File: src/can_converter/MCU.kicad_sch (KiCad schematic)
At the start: 12 parts, among them P2 CONN_01X02, U1 STM32G0B1CBT, X3 TC2030-NL, Y1 830108313809

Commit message: Add jst pa connector, replace tranciever, replace componenets, remove unneeded files
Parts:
- removed X3: TC2030-NL, Connector_Tag-Connect:TC2030-NL, symbol tag-connect:TC2030-NL
- added J102: IDC6, Bluesat:IDC6, symbol Connector_Generic:Conn_02x03_Odd_Even
- C1, C2: footprint Capacitor_SMD:C_0402_1005Metric_Pad0.74x0.62mm_HandSolder -> Capacitor_SMD:C_0402_1005Metric
- C3, C4, C5: footprint Capacitor_SMD:C_0603_1608Metric_Pad1.08x0.95mm_HandSolder -> Capacitor_SMD:C_0402_1005Metric
- R6: footprint Resistor_SMD:R_0402_1005Metric_Pad0.72x0.64mm_HandSolder -> Resistor_SMD:R_0402_1005Metric
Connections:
- net +3V3: now also J102.4 (Pin_4)
- net GND: now also J102.3 (Pin_3)
- net NRST: now also J102.6 (Pin_6)
- net SWCLK: now also J102.2 (Pin_2)
- net SWDIO: now also J102.1 (Pin_1)
- no-connect marks 28 -> 27

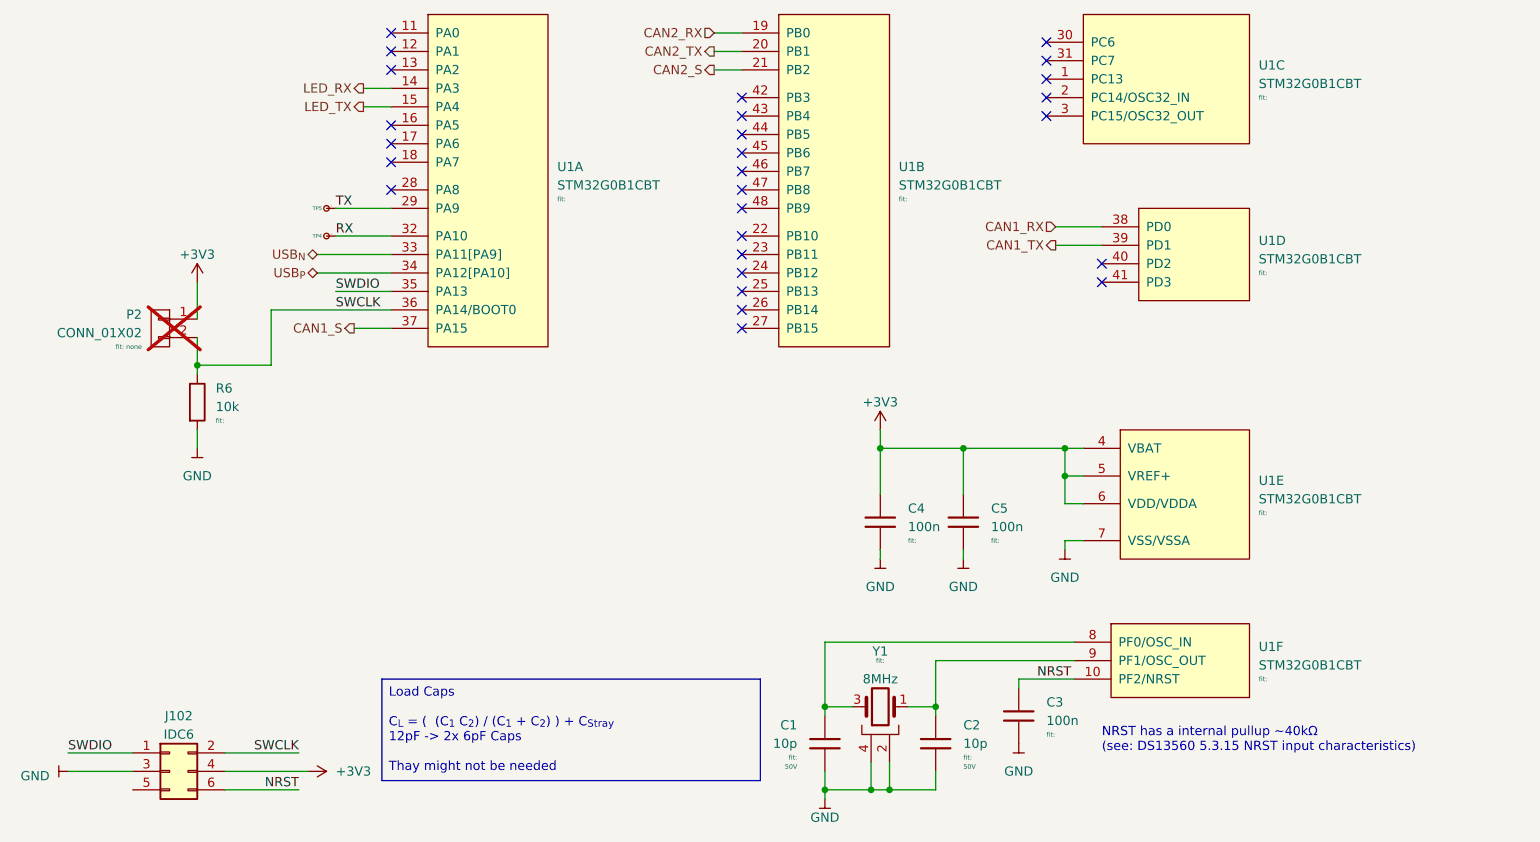
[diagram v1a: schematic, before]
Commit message: Remove lockfile, remove old debug header, route new debug header
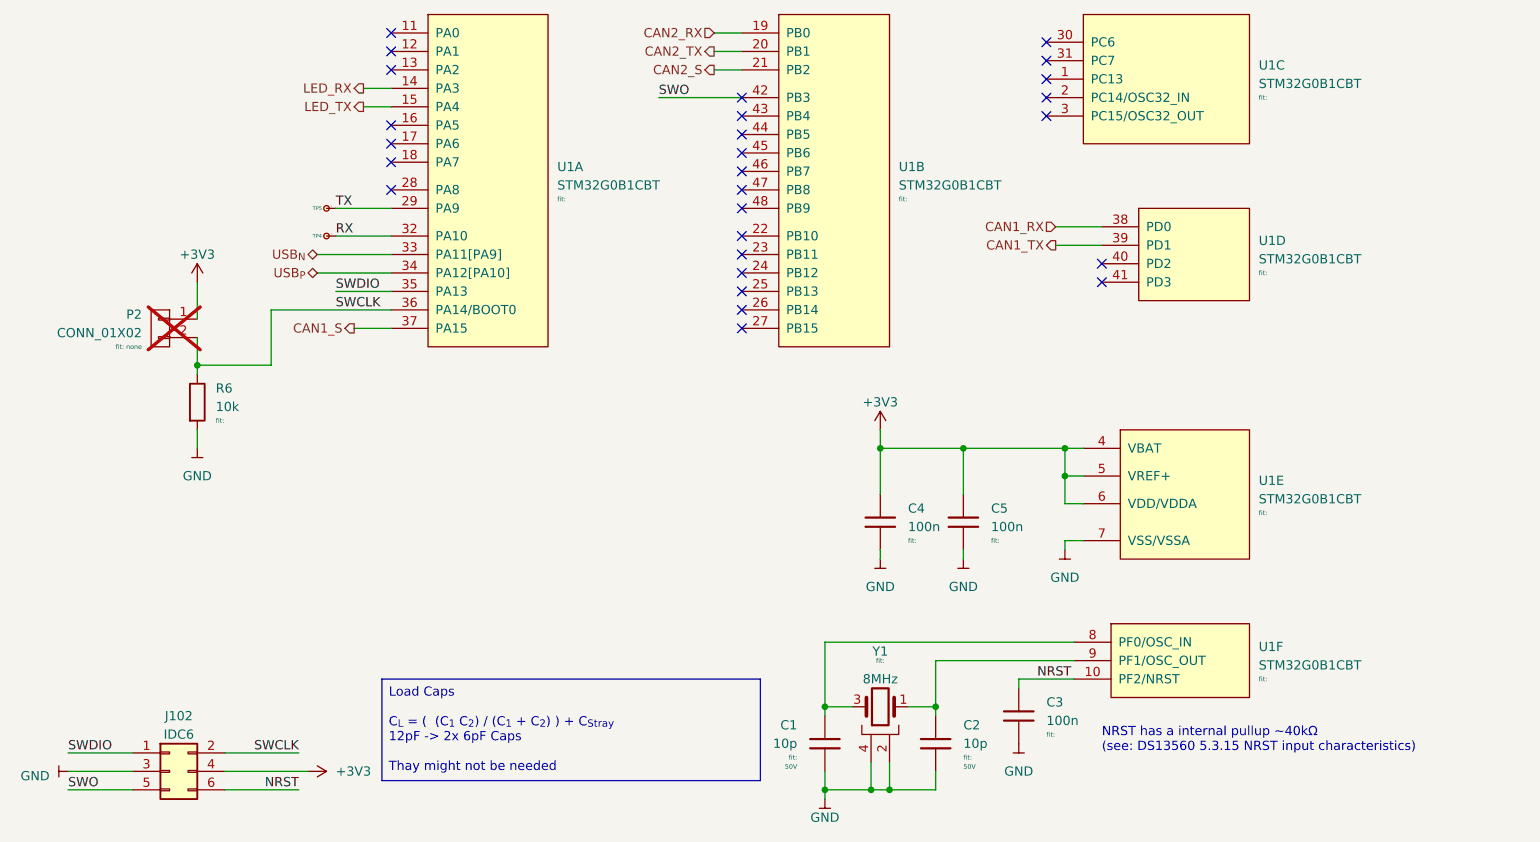
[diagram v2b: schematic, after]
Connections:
- net SWO: now reaches J102.5 (Pin_5)
- net SWO: now also U1.42 (PB3)
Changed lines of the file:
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@@
+	(wire
+		(pts
+			(xy 22.86 123.19) (xy 31.75 123.19)
+		)
+		(stroke
+			(width 0)
+			(type default)
+		)
+	)
 	(wire
 		(pts
@@
 		(pts
 			(xy 160.02 90.17) (xy 160.02 88.9)
+		)
+		(stroke
+			(width 0)
+			(type default)
+		)
+	)
+	(wire
+		(pts
+			(xy 104.14 27.94) (xy 115.57 27.94)
 		)
 		(stroke
@@
 		)
 	)
+	(label "SWO"
+		(at 22.86 123.19 0)
+		(effects
+			(font
+				(size 1.27 1.27)
+			)
+			(justify left bottom)
+		)
+	)
 	(label "SWDIO"
 		(at 59.69 54.61 0)
 		(effects
 			(font
+				(size 1.27 1.27)
+			)
+			(justify left bottom)
+		)
+	)
+	(label "SWO"
+		(at 104.14 27.94 0)
+		(effects
+			(font

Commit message: Finish layout and routing
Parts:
- removed P2: CONN_01X02, Connector_generic:Header_1x2_Pitch2.54mm, symbol generic-connectors:CONN_01X02
- C4: value 100n -> 220n; Package 0603 -> 0402
- C5: value 100n -> 220n
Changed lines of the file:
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@@
-	)
-	(junction
-		(at 40.64 64.77)
-		(diameter 0)
-		(color 0 0 0 0)
 	)
 	(junction
@@
 	(wire
 		(pts
-			(xy 40.64 64.77) (xy 50.8 64.77)
-		)
-		(stroke
-			(width 0)
-			(type default)
-		)
-	)
-	(wire
-		(pts
 			(xy 62.23 59.69) (xy 67.31 59.69)
 		)
@@
 	(wire
 		(pts
+			(xy 40.64 57.15) (xy 40.64 66.04)
+		)
+		(stroke
+			(width 0)
+			(type default)
+		)
+	)
+	(wire
+		(pts
 			(xy 63.5 29.21) (xy 67.31 29.21)
 		)
@@
 	(wire
 		(pts
-			(xy 50.8 64.77) (xy 50.8 57.15)
-		)
-		(stroke
-			(width 0)
-			(type default)
-		)
-	)
-	(wire
-		(pts
 			(xy 135.89 123.19) (xy 142.24 123.19)
 		)
@@
 	(wire
 		(pts
-			(xy 40.64 64.77) (xy 40.64 66.04)
-		)
-		(stroke
-			(width 0)
-			(type default)
-		)
-	)
-	(wire
-		(pts
 			(xy 44.45 118.11) (xy 54.61 118.11)
 		)
@@
 	(wire
 		(pts
-			(xy 50.8 57.15) (xy 67.31 57.15)
-		)
-		(stroke
-			(width 0)
-			(type default)
-		)
-	)
-	(wire
-		(pts
 			(xy 22.86 118.11) (xy 31.75 118.11)
 		)
@@
 	(wire
 		(pts
-			(xy 40.64 53.34) (xy 40.64 58.42)
-		)
-		(stroke
-			(width 0)
-			(type default)
-		)
-	)
-	(wire
-		(pts
 			(xy 160.02 83.82) (xy 160.02 80.01)
 		)
@@
 	(wire
 		(pts
-			(xy 40.64 60.96) (xy 40.64 64.77)
-		)
-		(stroke
-			(width 0)
-			(type default)
-		)
-	)
-	(wire
-		(pts
 			(xy 135.89 119.38) (xy 135.89 123.19)
 		)
@@
 		(pts
 			(xy 146.05 90.17) (xy 146.05 91.44)
+		)
+		(stroke
+			(width 0)
+			(type default)
+		)
+	)
+	(wire
+		(pts
+			(xy 40.64 57.15) (xy 67.31 57.15)
 		)
 		(stroke
@@
 	)
 	(symbol
-		(lib_id "generic-connectors:CONN_01X02")
-		(at 35.56 60.96 0)
-		(mirror y)
-		(unit 1)
-		(exclude_from_sim no)
-		(in_bom yes)
-		(on_board yes)
-		(dnp yes)
-		(fields_autoplaced yes)
-		(property "Reference" "P2"
-			(at 33.02 57.785 0)
-			(effects
-				(font
-					(size 1.27 1.27)
-				)
-				(justify left)
-			)
-		)
-		(property "Value" "CONN_01X02"
-			(at 33.02 60.325 0)
-			(effects
-				(font
-					(size 1.27 1.27)
-				)
-				(justify left)
-			)
-		)
-		(property "Footprint" "Connector_generic:Header_1x2_Pitch2.54mm"
-			(at 46.99 54.61 0)
-			(effects
-				(font
-					(size 1.27 1.27)
-				)
-				(hide yes)
-			)
-		)
-		(property "Datasheet" ""
-			(at 35.56 55.88 0)
-			(effects
-				(font
-					(size 1.27 1.27)
-				)
-			)
-		)
-		(property "Description" ""
-			(at 35.56 60.96 0)
-			(effects
-				(font
-					(size 1.27 1.27)
-				)
-			)
-		)
-		(property "Manufacturer" "generic"
-			(at 33.02 53.34 0)
-			(effects
-				(font
-					(size 1.524 1.524)
-				)
-				(hide yes)
-			)
-		)
-		(property "MPN" "generic"
-			(at 30.48 50.8 0)
-			(effects
-				(font
-					(size 1.524 1.524)
-				)
-				(hide yes)
-			)
-		)
-		(property "Fit" "fit: none"
-			(at 33.02 62.23 0)
-			(effects
-				(font
-					(size 0.635 0.635)
-				)
-				(justify left)
-			)
-		)
-		(property "State" "legacy"
-			(at 27.94 64.77 0)
-			(effects
-				(font
-					(size 0.635 0.635)
-				)
-				(hide yes)
-			)
-		)
-		(property "Package" "THT 2.54mm 1x2-pin"
-			(at 35.56 60.96 0)
-			(effects
-				(font
-					(size 0.635 0.635)
-				)
-				(hide yes)
-			)
-		)
-		(pin "1"
-		)
-		(pin "2"
-		)
-		(instances
-			(project "candleLightfd-S01"
-				(path "/e63e39d7-6ac0-4ffd-8aa3-1841a4541b55/c754f27f-d753-4109-9c59-639a39396c66"
-					(reference "P2")
-					(unit 1)
-				)
-			)
-		)
-	)
-	(symbol
 		(lib_id "powerport:GND")
 		(at 146.05 91.44 0)
@@
 			)
 		)
-		(property "Value" "100n"
+		(property "Value" "220n"
 			(at 138.43 87.0077 0)
 			(effects
@@
 			)
 		)
-		(property "Package" "0603"
+		(property "Package" "0402"
 			(at 134.62 86.36 0)
 			(effects
@@
 			)
 		)
-		(property "Value" "100n"
+		(property "Value" "220n"
 			(at 149.86 87.0077 0)
 			(effects
@@
 					(unit 1)
 				)
-			)
-		)
-	)
-	(symbol
-		(lib_id "powerport:+3V3")
-		(at 40.64 53.34 0)
-		(unit 1)
-		(exclude_from_sim no)
-		(in_bom yes)
-		(on_board yes)
-		(dnp no)
-		(fields_autoplaced yes)
-		(property "Reference" "#PWR017"
-			(at 40.64 57.15 0)
-			(effects
-				(font
-					(size 1.27 1.27)
-				)
-				(hide yes)
-			)
-		)
-		(property "Value" "+3V3"
-			(at 40.64 49.53 0)
-			(effects
-				(font
-					(size 1.27 1.27)
-				)
-			)
-		)
-		(property "Footprint" ""
-			(at 40.64 53.34 0)
-			(effects
-				(font
-					(size 1.27 1.27)
-				)
-			)
-		)
-		(property "Datasheet" ""
-			(at 40.64 53.34 0)
-			(effects
-				(font
-					(size 1.27 1.27)
-				)
-			)
-		)
-		(property "Description" ""
-			(at 40.64 53.34 0)
-			(effects
-				(font
-					(size 1.27 1.27)
-				)
-			)
-		)
-		(pin "1"
-		)
-		(instances
-			(project "candleLightfd-S01"
-				(path "/e63e39d7-6ac0-4ffd-8aa3-1841a4541b55/c754f27f-d753-4109-9c59-639a39396c66"
-					(reference "#PWR017")
-					(unit 1)
-				)
